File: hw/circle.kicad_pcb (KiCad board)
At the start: 2 copper layers, 46 x 46 mm, 50 parts, among them J1 CONN_01X02, J2 USB_OTG, J3 CONN_01X03, J4 CONN_02X05, J5 CONN_01X03, J6 CONN_01X06, U1 STM32F303CCTx, U2 AS5048A, U3 DRV8312, U4 INA240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

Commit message: mounting holes
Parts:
- moved J5 2.77 mm to (80.5, 92.0), turned to 150 degrees
- moved C16 2.00 mm to (84.0, 105.0)
- moved C17 2.00 mm to (92.8, 107.0)
- moved C18 2.00 mm to (87.0, 95.0)
- moved C19 2.00 mm to (96.0, 100.0)
- moved U1 2.00 mm to (90.0, 101.0)
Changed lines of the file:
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@@
     (links 178)
     (no_connects 178)
-    (area 72.624999 73.038032 140.675001 126.0925)
+    (area 59.899999 69.899999 140.675001 135.100001)
     (thickness 1.6)
-    (drawings 1)
+    (drawings 14)
     (tracks 0)
     (zones 0)
@@
     (47 F.CrtYd user)
     (48 B.Fab user hide)
-    (49 F.Fab user hide)
+    (49 F.Fab user)
   )
   (setup
@@
     (zone_45_only no)
     (trace_min 0.2)
-    (segment_width 0.2)
+    (segment_width 0.5)
     (edge_width 0.15)
     (via_size 0.8)
@@
     (fp_line (start 2.85 -1.15) (end -1.6 -1.15) (layer F.CrtYd) (width 0.05))
     (fp_line (start 2.85 6.25) (end 2.85 -1.15) (layer F.CrtYd) (width 0.05))
-    (fp_line (start -1.6 6.25) (end 2.85 6.25) (layer F.CrtYd) (width 0.05))
-    (fp_line (start -1.6 -1.15) (end -1.6 6.25) (layer F.CrtYd) (width 0.05))
-    (fp_line (start -1.13 -0.695) (end 0 -0.695) (layer F.SilkS) (width 0.12))
-    (fp_line (start -1.13 0) (end -1.13 -0.695) (layer F.SilkS) (width 0.12))
+    (fp_line (start -1.6 6.249999) (end 2.85 6.25) (layer F.CrtYd) (width 0.05))
+    (fp_line (start -1.6 -1.15) (end -1.6 6.249999) (layer F.CrtYd) (width 0.05))
+    (fp_line (start -1.13 -0.695001) (end 0 -0.695) (layer F.SilkS) (width 0.12))
+    (fp_line (start -1.13 0) (end -1.13 -0.695001) (layer F.SilkS) (width 0.12))
     (fp_line (start 0.635 0.635) (end -1.13 0.635) (layer F.SilkS) (width 0.12))
     (fp_line (start 0.635 -0.695) (end 0.635 0.635) (layer F.SilkS) (width 0.12))
@@
     (pad 5 thru_hole oval (at 0 10.16 110) (size 1.7 1.7) (drill 1) (layers *.Cu *.Mask)
       (net 57 /RS485A))
-    (pad 4 thru_hole oval (at 0 7.62 110) (size 1.7 1.7) (drill 1) (layers *.Cu *.Mask)
+    (pad 4 thru_hole oval (at -0.000001 7.62 110) (size 1.7 1.7) (drill 1) (layers *.Cu *.Mask)
       (net 56 /RS485B))
     (pad 3 thru_hole oval (at 0 5.079999 110) (size 1.7 1.7) (drill 1) (layers *.Cu *.Mask)
@@
   )
   (module Pin_Headers:Pin_Header_Angled_1x03_Pitch2.54mm (layer F.Cu)
-    (at 83.25 92.29 180)
+    (at 80.5 92 150)
     (descr "Through hole angled pin header, 1x03, 2.54mm pitch, 6mm pin length, single row")
     (tags "Through hole angled pin header THT 1x03 2.54mm single row")
-    (fp_text reference J5 (at 4.315 -2.27 180) (layer F.SilkS)
-      (effects (font (size 1 1) (thickness 0.15)))
-    )
-    (fp_text value CONN_01X03 (at 4.315 7.35 180) (layer F.Fab)
-      (effects (font (size 1 1) (thickness 0.15)))
-    )
-    (fp_text user %R (at 4.315 -2.27 180) (layer F.Fab)
+    (fp_text reference J5 (at 4.315 -2.27 150) (layer F.SilkS)
+      (effects (font (size 1 1) (thickness 0.15)))
+    )
+    (fp_text value CONN_01X03 (at 4.315 7.35 150) (layer F.Fab)
+      (effects (font (size 1 1) (thickness 0.15)))
+    )
+    (fp_text user %R (at 4.315 -2.27 150) (layer F.Fab)
       (effects (font (size 1 1) (thickness 0.15)))
     )
@@
     (fp_line (start 1.4 1.27) (end 3.9 1.27) (layer F.Fab) (width 0.1))
     (fp_line (start 1.4 -1.27) (end 1.4 1.27) (layer F.Fab) (width 0.1))
-    (pad 3 thru_hole oval (at 0 5.08 180) (size 1.7 1.7) (drill 1) (layers *.Cu *.Mask)
-      (net 14 GND))
-    (pad 2 thru_hole oval (at 0 2.54 180) (size 1.7 1.7) (drill 1) (layers *.Cu *.Mask)
+    (pad 3 thru_hole oval (at 0 5.08 150) (size 1.7 1.7) (drill 1) (layers *.Cu *.Mask)
+      (net 14 GND))
+    (pad 2 thru_hole oval (at 0 2.54 150) (size 1.7 1.7) (drill 1) (layers *.Cu *.Mask)
       (net 62 /STDIN))
-    (pad 1 thru_hole rect (at 0 0 180) (size 1.7 1.7) (drill 1) (layers *.Cu *.Mask)
+    (pad 1 thru_hole rect (at 0 0 150) (size 1.7 1.7) (drill 1) (layers *.Cu *.Mask)
       (net 63 /STDOUT))
     (model ${KISYS3DMOD}/Pin_Headers.3dshapes/Pin_Header_Angled_1x03_Pitch2.54mm.wrl
@@
   )
   (module Capacitors_SMD:C_0603 (layer F.Cu)
-    (at 96 98 90)
+    (at 96 100 90)
     (descr "Capacitor SMD 0603, reflow soldering, AVX (see smccp.pdf)")
     (tags "capacitor 0603")
@@
   )
   (module Capacitors_SMD:C_0603 (layer F.Cu)
-    (at 87 93 180)
+    (at 87 95 180)
     (descr "Capacitor SMD 0603, reflow soldering, AVX (see smccp.pdf)")
     (tags "capacitor 0603")
@@
   )
   (module Capacitors_SMD:C_0603 (layer F.Cu)
-    (at 92.75 105)
+    (at 92.75 107)
     (descr "Capacitor SMD 0603, reflow soldering, AVX (see smccp.pdf)")
     (tags "capacitor 0603")
@@
   )
   (module Capacitors_SMD:C_0603 (layer F.Cu)
-    (at 84 103 270)
+    (at 84 105 270)
     (descr "Capacitor SMD 0603, reflow soldering, AVX (see smccp.pdf)")
     (tags "capacitor 0603")
@@
   )
   (module Housings_QFP:LQFP-48_7x7mm_Pitch0.5mm (layer F.Cu)
-    (at 90 99 180)
+    (at 90 101 180)
     (descr "48 LEAD LQFP 7x7mm (see MICREL LQFP7x7-48LD-PL-1.pdf)")
     (tags "QFP 0.5")
@@
     )
   )
+  (gr_circle (center 113.86 92) (end 113.86 90.5) (layer Dwgs.User) (width 0.5))
+  (gr_circle (center 86.144 92) (end 86.144 90.5) (layer Dwgs.User) (width 0.5))
+  (gr_circle (center 100 116) (end 98.5 116.5) (layer Dwgs.User) (width 0.5))
+  (gr_circle (center 87.5 100) (end 87.5 101) (layer Dwgs.User) (width 0.2))
+  (gr_circle (center 112.5 100) (end 112.5 101) (layer Dwgs.User) (width 0.2))
+  (gr_circle (center 100 109.5) (end 101 109.5) (layer Dwgs.User) (width 0.2))
+  (gr_circle (center 100 90.5) (end 101 90.5) (layer Dwgs.User) (width 0.2))
+  (gr_circle (center 92 100) (end 92 101) (layer Dwgs.User) (width 0.2))
+  (gr_circle (center 108 100) (end 108 101) (layer Dwgs.User) (width 0.2))
+  (gr_line (start 100 135) (end 100 135) (layer Dwgs.User) (width 0.2))
+  (gr_line (start 100 70) (end 100 135) (layer Dwgs.User) (width 0.2))
+  (gr_line (start 140 100) (end 140 100) (layer Dwgs.User) (width 0.2))
+  (gr_line (start 60 100) (end 140 100) (layer Dwgs.User) (width 0.2))
   (gr_circle (center 100 100) (end 123 100) (layer Edge.Cuts) (width 0.15))
 )

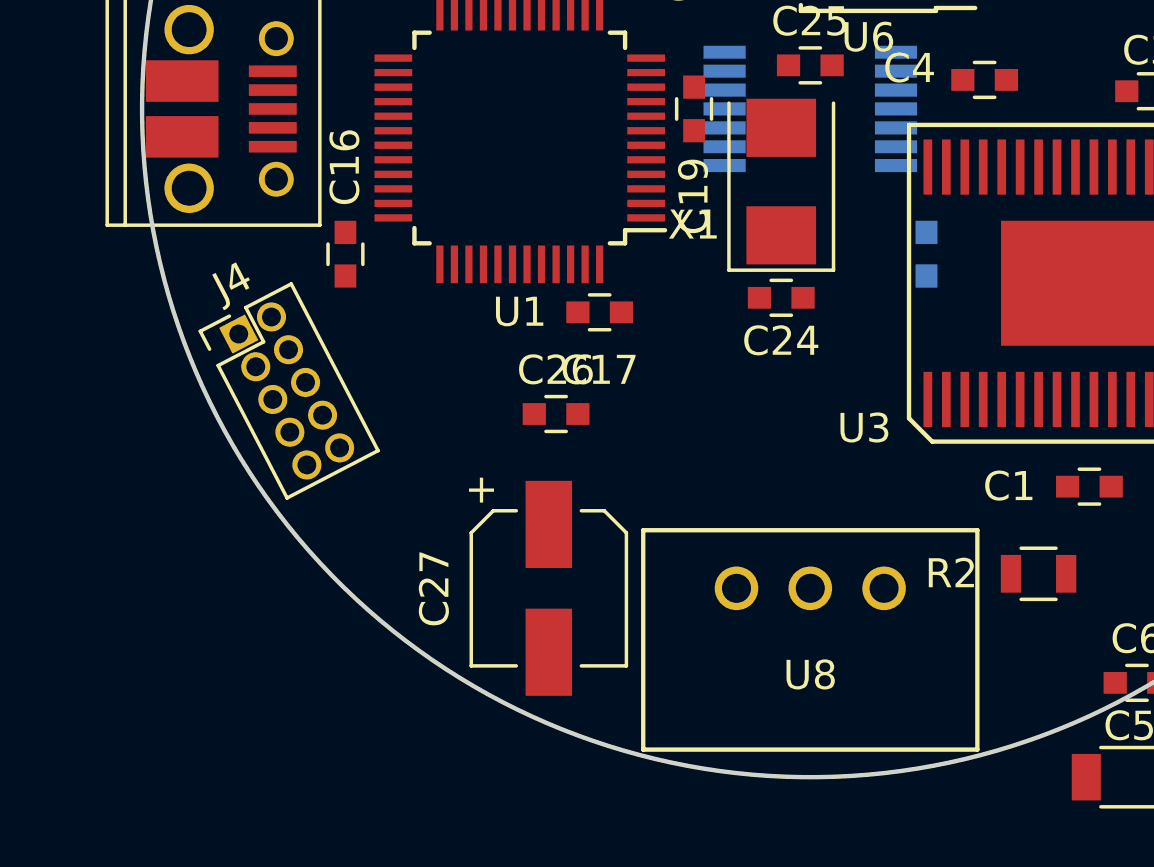
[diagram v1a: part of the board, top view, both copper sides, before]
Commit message: moving placements a bit to clear mounting holes
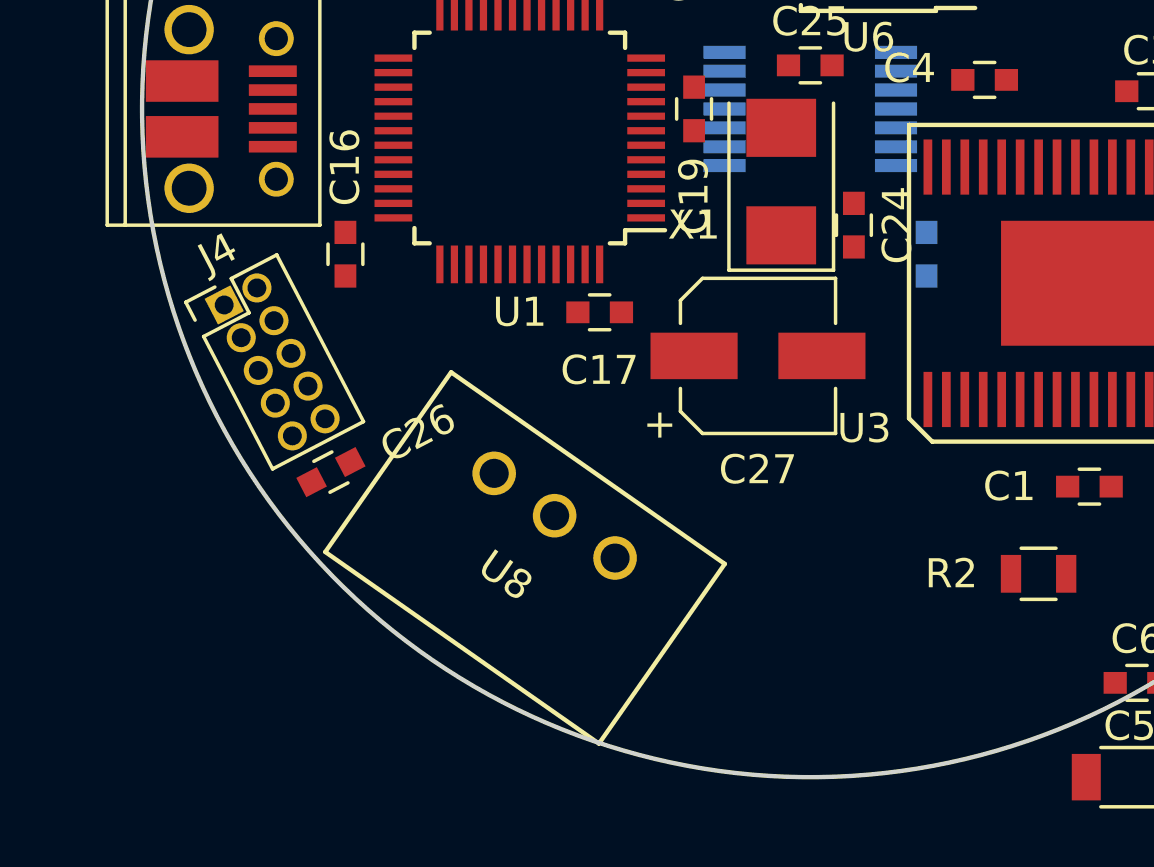
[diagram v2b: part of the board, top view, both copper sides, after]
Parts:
- moved C27 10.8 mm to (98.2, 108.5), turned to 0 degrees
- moved U8 9.15 mm to (91.2, 114.0), turned to 145 degrees
- moved C26 8.00 mm to (83.5, 112.5), turned to 27.5 degrees
- moved C24 3.54 mm to (101.5, 104.0), turned to 270 degrees
- moved J4 1.12 mm to (79.8, 106.7)
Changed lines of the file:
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@@
-(kicad_pcb (version 20170123) (host pcbnew no-vcs-found-f007601~58~ubuntu16.04.1)
+(kicad_pcb (version 20170123) (host pcbnew no-vcs-found-02abf18~58~ubuntu16.04.1)
   (general
     (links 178)
@@
     (47 F.CrtYd user)
     (48 B.Fab user hide)
-    (49 F.Fab user)
+    (49 F.Fab user hide)
   )
   (setup
@@
   )
   (module Capacitors_SMD:CP_Elec_5x5.8 (layer F.Cu)
-    (at 91 116.5 270)
+    (at 98.2 108.5)
     (descr "SMT capacitor, aluminium electrolytic, 5x5.8")
     (attr smd)
-    (fp_text reference C27 (at 0 3.92 270) (layer F.SilkS)
-      (effects (font (size 1 1) (thickness 0.15)))
-    )
-    (fp_text value 100u (at 0 -3.92 270) (layer F.Fab)
+    (fp_text reference C27 (at 0 3.92) (layer F.SilkS)
+      (effects (font (size 1 1) (thickness 0.15)))
+    )
+    (fp_text value 100u (at 0 -3.92) (layer F.Fab)
       (effects (font (size 1 1) (thickness 0.15)))
     )
@@
     (fp_line (start -1.84 2.51) (end 2.51 2.51) (layer F.Fab) (width 0.1))
     (fp_line (start 2.51 2.51) (end 2.51 -2.51) (layer F.Fab) (width 0.1))
-    (fp_text user %R (at 0 3.92 270) (layer F.Fab)
-      (effects (font (size 1 1) (thickness 0.15)))
-    )
-    (fp_text user + (at -3.38 2.35 270) (layer F.SilkS)
-      (effects (font (size 1 1) (thickness 0.15)))
-    )
-    (fp_text user + (at -1.38 -0.06 270) (layer F.Fab)
+    (fp_text user %R (at 0 3.92) (layer F.Fab)
+      (effects (font (size 1 1) (thickness 0.15)))
+    )
+    (fp_text user + (at -3.38 2.35) (layer F.SilkS)
+      (effects (font (size 1 1) (thickness 0.15)))
+    )
+    (fp_text user + (at -1.38 -0.06) (layer F.Fab)
       (effects (font (size 1 1) (thickness 0.15)))
     )
     (fp_circle (center 0 0) (end 0.1 2.4) (layer F.Fab) (width 0.1))
-    (pad 2 smd rect (at 2.2 0 90) (size 3 1.6) (layers F.Cu F.Paste F.Mask)
-      (net 14 GND))
-    (pad 1 smd rect (at -2.2 0 90) (size 3 1.6) (layers F.Cu F.Paste F.Mask)
+    (pad 2 smd rect (at 2.2 0 180) (size 3 1.6) (layers F.Cu F.Paste F.Mask)
+      (net 14 GND))
+    (pad 1 smd rect (at -2.2 0 180) (size 3 1.6) (layers F.Cu F.Paste F.Mask)
       (net 1 +3V3))
     (model Capacitors_SMD.3dshapes/CP_Elec_5x5.8.wrl
@@
   )
   (module Pin_Headers:Pin_Header_Straight_2x05_Pitch1.27mm (layer F.Cu)
-    (at 80.327159 107.746992 27.5)
+    (at 79.827159 106.746992 27.5)
     (descr "Through hole straight pin header, 2x05, 1.27mm pitch, double rows")
     (tags "Through hole pin header THT 2x05 1.27mm double row")
@@
   )
   (module Capacitors_SMD:C_0603 (layer F.Cu)
-    (at 91.25 110.5)
+    (at 83.5 112.5 27.5)
     (descr "Capacitor SMD 0603, reflow soldering, AVX (see smccp.pdf)")
     (tags "capacitor 0603")
     (attr smd)
-    (fp_text reference C26 (at 0 -1.5) (layer F.SilkS)
-      (effects (font (size 1 1) (thickness 0.15)))
-    )
-    (fp_text value 100n (at 0 1.5) (layer F.Fab)
+    (fp_text reference C26 (at 3.275396 0.205064 27.5) (layer F.SilkS)
+      (effects (font (size 1 1) (thickness 0.15)))
+    )
+    (fp_text value 100n (at 0 1.5 27.5) (layer F.Fab)
       (effects (font (size 1 1) (thickness 0.15)))
     )
@@
     (fp_line (start 0.8 0.4) (end -0.8 0.4) (layer F.Fab) (width 0.1))
     (fp_line (start -0.8 0.4) (end -0.8 -0.4) (layer F.Fab) (width 0.1))
-    (fp_text user %R (at 0 -1.5) (layer F.Fab)
-      (effects (font (size 1 1) (thickness 0.15)))
-    )
-    (pad 2 smd rect (at 0.75 0) (size 0.8 0.75) (layers F.Cu F.Paste F.Mask)
+    (fp_text user %R (at 0 -1.5 27.5) (layer F.Fab)
+      (effects (font (size 1 1) (thickness 0.15)))
+    )
+    (pad 2 smd rect (at 0.75 0 27.5) (size 0.8 0.75) (layers F.Cu F.Paste F.Mask)
       (net 66 /NRST))
-    (pad 1 smd rect (at -0.75 0) (size 0.8 0.75) (layers F.Cu F.Paste F.Mask)
+    (pad 1 smd rect (at -0.75 0 27.5) (size 0.8 0.75) (layers F.Cu F.Paste F.Mask)
       (net 14 GND))
     (model Capacitors_SMD.3dshapes/C_0603.wrl
@@
   )
   (module Capacitors_SMD:C_0603 (layer F.Cu)
-    (at 99 106.5 180)
+    (at 101.5 104 270)
     (descr "Capacitor SMD 0603, reflow soldering, AVX (see smccp.pdf)")
     (tags "capacitor 0603")
     (attr smd)
-    (fp_text reference C24 (at 0 -1.5 180) (layer F.SilkS)
-      (effects (font (size 1 1) (thickness 0.15)))
-    )
-    (fp_text value 12p (at 0 1.5 180) (layer F.Fab)
-      (effects (font (size 1 1) (thickness 0.15)))
-    )
-    (fp_text user %R (at 0 -1.5 180) (layer F.Fab)
+    (fp_text reference C24 (at 0 -1.5 270) (layer F.SilkS)
+      (effects (font (size 1 1) (thickness 0.15)))
+    )
+    (fp_text value 12p (at 0 1.5 270) (layer F.Fab)
+      (effects (font (size 1 1) (thickness 0.15)))
+    )
+    (fp_text user %R (at 0 -1.5 270) (layer F.Fab)
       (effects (font (size 1 1) (thickness 0.15)))
     )
@@
     (fp_line (start 1.4 0.65) (end 1.4 -0.65) (layer F.CrtYd) (width 0.05))
     (fp_line (start 1.4 0.65) (end -1.4 0.65) (layer F.CrtYd) (width 0.05))
-    (pad 1 smd rect (at -0.75 0 180) (size 0.8 0.75) (layers F.Cu F.Paste F.Mask)
-      (net 14 GND))
-    (pad 2 smd rect (at 0.75 0 180) (size 0.8 0.75) (layers F.Cu F.Paste F.Mask)
+    (pad 1 smd rect (at -0.75 0 270) (size 0.8 0.75) (layers F.Cu F.Paste F.Mask)
+      (net 14 GND))
+    (pad 2 smd rect (at 0.75 0 270) (size 0.8 0.75) (layers F.Cu F.Paste F.Mask)
       (net 68 /OSC_IN))
     (model Capacitors_SMD.3dshapes/C_0603.wrl
@@
   )
   (module DCDC:R-78xx-0.5 (layer F.Cu)
-    (at 100 116.5 180)
-    (fp_text reference U8 (at 0 -3 180) (layer F.SilkS)
-      (effects (font (size 1 1) (thickness 0.15)))
-    )
-    (fp_text value R-78xx-0.5 (at 0 -2.54 180) (layer F.Fab)
-      (effects (font (size 1 1) (thickness 0.15)))
-    )
-    (fp_line (start -5.75 2) (end -5.75 -5.55) (layer F.SilkS) (width 0.15))
-    (fp_line (start -5.75 2) (end 5.75 2) (layer F.SilkS) (width 0.15))
-    (fp_line (start -5.75 -5.55) (end 5.75 -5.55) (layer F.SilkS) (width 0.15))
-    (fp_line (start 5.75 -5.55) (end 5.75 2) (layer F.SilkS) (width 0.15))
-    (pad 3 thru_hole circle (at 2.54 0 180) (size 1.5 1.5) (drill 1) (layers *.Cu *.Mask)
+    (at 91.199705 114 145)
+    (fp_text reference U8 (at 0.197064 -2.658676 145) (layer F.SilkS)
+      (effects (font (size 1 1) (thickness 0.15)))
+    )
+    (fp_text value R-78xx-0.5 (at 0 -2.54 145) (layer F.Fab)
+      (effects (font (size 1 1) (thickness 0.15)))
+    )
+    (fp_line (start -5.75 2.000001) (end -5.75 -5.550001) (layer F.SilkS) (width 0.15))
+    (fp_line (start -5.75 2.000001) (end 5.750001 2.000001) (layer F.SilkS) (width 0.15))
+    (fp_line (start -5.75 -5.550001) (end 5.75 -5.550001) (layer F.SilkS) (width 0.15))
+    (fp_line (start 5.75 -5.550001) (end 5.750001 2.000001) (layer F.SilkS) (width 0.15))
+    (pad 3 thru_hole circle (at 2.54 0 145) (size 1.5 1.5) (drill 1) (layers *.Cu *.Mask)
       (net 1 +3V3))
-    (pad 2 thru_hole circle (at 0 0 180) (size 1.5 1.5) (drill 1) (layers *.Cu *.Mask)
-      (net 14 GND))
-    (pad 1 thru_hole circle (at -2.54 0 180) (size 1.5 1.5) (drill 1) (layers *.Cu *.Mask)
+    (pad 2 thru_hole circle (at 0 0 145) (size 1.5 1.5) (drill 1) (layers *.Cu *.Mask)
+      (net 14 GND))
+    (pad 1 thru_hole circle (at -2.54 0 145) (size 1.5 1.5) (drill 1) (layers *.Cu *.Mask)
       (net 19 +12V))
   )

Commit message: initial placement complete
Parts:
- C13, C28: value 220u -> 100u; footprint Capacitors_SMD:CP_Elec_6.3x7.7 -> Capacitors_SMD:CP_Elec_5x5.8
- moved C28 35.8 mm to (105.0, 119.5), turned to 15 degrees
- moved C12 26.7 mm to (106.0, 98.5), turned to 270 degrees
- moved C9 26.4 mm to (102.5, 103.2), turned to 90 degrees
- moved C11 17.4 mm to (111.5, 98.5), turned to 270 degrees
- moved C8 16.6 mm to (104.5, 114.0)
- moved C10 10.8 mm to (115.0, 98.5), turned to 270 degrees
- moved C5 10.3 mm to (116.0, 114.0), turned to 50 degrees
- moved C6 9.90 mm to (104.5, 112.5)
- moved C7 6.27 mm to (119.0, 109.5), turned to 270 degrees
- moved C13 6.26 mm to (119.5, 96.0), turned to 100 degrees
- moved J1 4.50 mm to (120.0, 105.5)
- moved J4 4.16 mm to (83.5, 108.7), turned to 0 degrees
- moved C2 3.95 mm to (114.5, 95.5)
- moved C3 3.58 mm to (110.5, 96.0)
- moved C24 3.54 mm to (99.0, 106.5), turned to 180 degrees
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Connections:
- J1 pad 1: +12V -> GND
- J1 pad 2: GND -> +12V
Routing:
- net (no net): vias 0 -> 3

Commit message: power planes
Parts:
- moved C2 3.61 mm to (116.5, 98.5), turned to 270 degrees
- moved C14 1.50 mm to (100.5, 87.0)
- moved C20 1.00 mm to (102.0, 87.0)
- moved U4 1.00 mm to (107.0, 87.0)
- moved R3 0.75 mm to (112.0, 87.0)
- moved U5 0.54 mm to (104.5, 91.0)
- moved R4 0.50 mm to (109.5, 91.0)
- moved C13 0.22 mm to (119.7, 96.1)
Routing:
- net (no net): track 0.00 -> 0.35 mm, vias 3 -> 4
- added copper zone on In2.Cu, net +12V
- added copper zone on In2.Cu, net +3V3
- added copper zone on In1.Cu, net GND
- added copper zone on In2.Cu, net VAA
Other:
- copper layers 2 -> 4
- rule trace_min: 0.2 -> 0.1524
- rule via_min_drill: 0.3 -> 0.254
- rule via_min_size: 0.4 -> 0.5588

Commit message: routing
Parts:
- moved L1 6.62 mm to (97.5, 86.0)
- moved R6 4.43 mm to (90.2, 84.7), turned to 30 degrees
- moved J6 4.40 mm to (83.6, 86.0), turned to 120 degrees
- moved C23 3.55 mm to (89.2, 88.2), turned to 120 degrees
- moved J5 2.69 mm to (79.5, 94.5), turned to 160 degrees
- moved U7 2.37 mm to (92.2, 88.2), turned to 120 degrees
- moved J3 1.94 mm to (111.7, 83.0), turned to 155 degrees
- moved C28 1.12 mm to (106.0, 119.0)
- moved C18 0.71 mm to (83.5, 95.5), turned to 0 degrees
- moved C26 0.71 mm to (85.5, 116.0), turned to 135 degrees
- moved R1 0.61 mm to (112.0, 113.5)
- moved C12 0.56 mm to (105.8, 99.0)
- moved C16 0.50 mm to (85.5, 106.5)
- moved C17 0.50 mm to (93.5, 106.5)
- moved C21 0.50 mm to (99.5, 91.0)
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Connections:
- J2 pad 6: Net-(J2-Pad6) -> GND
- J5 pad 1: /STDOUT -> /STDIN
- J5 pad 2: /STDIN -> /STDOUT
- J6 pad 2: GND -> /RS485B
- J6 pad 4: /RS485B -> /RS485A
- J6 pad 6: /RS485A -> GND
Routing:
- net /PWMA: track 0.00 -> 41.4 mm
- net /PWMB: track 0.00 -> 39.0 mm
- net GND: track 0.00 -> 38.8 mm, vias 0 -> 19
- net /PWMC: track 0.00 -> 26.3 mm
- net /NRST: track 0.00 -> 25.4 mm, vias 0 -> 1
- net /AMPA: track 0.00 -> 18.2 mm
- net +3V3: track 0.00 -> 17.4 mm, vias 0 -> 6
- net /RS485RE: track 0.00 -> 16.4 mm
- net /OUTC: track 0.00 -> 15.2 mm
- net +12V: track 0.00 -> 15.0 mm, vias 0 -> 3
- net /RS485DE: track 0.00 -> 13.9 mm
- net /SENSEC: track 0.00 -> 13.2 mm
- net /AMPB: track 0.00 -> 12.0 mm
- net /OUTB: track 0.00 -> 11.8 mm
- net VAA: track 0.00 -> 11.5 mm, vias 0 -> 3
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- added copper zone on F.Cu, net +12V
- added copper zone on F.Cu, net +3V3
- added copper zone on F.Cu, net /OUTA
- added copper zone on F.Cu, net /OUTB
- added copper zone on F.Cu, net /OUTC
- added copper zone on F.Cu, net /SENSEA
- added copper zone on F.Cu, net VAA
